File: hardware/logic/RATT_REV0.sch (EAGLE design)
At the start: 97 parts, among them IC1 TLP292-4, J3 F-1X06-SIP-100-40, J5 F-1X02-SIP-100-40, Q1 2.5A/30V, Q2 MBT3904DW1T1, Q3 2.5A/30V, Q5 2N7002, Q6 2.5A/30V, U3 MCP73831, U5 AP2112K-3.3V, U6 PCA9539PW

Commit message: All sorts of shit
I/Os are done, connectors, protections, options all added.  Screen updated, library updated, very close to layout ready.
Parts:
- added D10, D2, D5, D6, D7, D8, D9: BAT54S, DURRIDGE-DIODES:BAT54S
- added IC2, IC3, IC4, IC5: CPC1002N, MakeItLabs:CPC1002N
- added J1, J2, J4, J6: (no value), MakeItLabs:GROVE-CONNECTOR-TH-RA
- added J7, J8: PHOENIX1803484, MakeItLabs:PHOENIX1803484
- added JP1: (no value), pinhead:PINHD-2X8
- added LED1, LED2: (no value), SparkFun-LED:LED5MM
- added LED3: RED, SparkFun-LED:LED-RED0603
- added R41, R42: 680R, SparkFun-Resistors:RESISTOR0603-RES
- added R43, R44, R45, R46, R47, R48, R49, R50: 100R, SparkFun-Resistors:RESISTOR0603-RES
- added R51, R52, R53, R54: 680R, SparkFun-Passives:RESISTOR0603-RES
- D3: value RED -> BAT54S; device SparkFun-LED:LED-RED0603 -> DURRIDGE-DIODES:BAT54S
- LCD1: device MakeIt_Labs:1.8TFT_ADA -> MakeItLabs:1.8TFT_ADA
- LCD3: device MakeIt_Labs:1.8TFT_CHI2.0 -> MakeItLabs:1.8TFT_CHI2.0
- renumbered U$1 to U1, U3 to IC13, U6 to IC16
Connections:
- new net N$48: LED1.A, R41.1
- new net N$49: LED2.A, R42.1
- new net N$50: J2.1, R43.2
- new net N$51: J2.2, R44.2
- new net N$52: J1.1, R45.2
- new net N$53: J1.2, R46.2
- new net N$54: J4.1, R47.2
- new net N$55: J4.2, R48.2
- new net N$56: J6.1, R49.2
- new net N$57: J6.2, R50.2
- new net N$58: IC2.ANODE, R51.1
- new net N$59: IC2.DC+, J8.1.1
- new net N$60: IC2.DC-, J8.2.1
- new net N$61: IC3.ANODE, R52.1
- new net N$62: IC3.DC+, J8.3.1
- new net N$63: IC3.DC-, J8.4.1
- new net N$64: IC4.DC+, J8.5.1
- new net N$65: IC4.DC-, J8.6.1
- new net N$66: IC5.DC+, J8.7.1
- new net N$67: IC5.DC-, J8.8.1
- new net N$68: IC4.ANODE, R53.1
- new net N$69: IC5.ANODE, R54.1
- net +3V3: now also JP1.3, R41.2, R42.2
- net +5V: now also D10.C2, D2.C2, D3.C2, D5.C2, D6.C2, D7.C2, D8.C2, D9.C2, J1.3, J2.3, J4.3, J6.3, JP1.5
- net GND: now also D10.A1, D2.A1, D3.A1, D5.A1, D6.A1, D7.A1, D8.A1, D9.A1, IC2.CATHODE, IC3.CATHODE, IC4.CATHODE, IC5.CATHODE, J1.4, J2.4, J4.4, J6.4, JP1.1, JP1.7, LED3.C; no longer D3.C
- net I2C_SCL: now also JP1.9
- net I2C_SDA: now also JP1.11
- net IN0: now also D6.C1A2, JP1.2, R45.1
- net IN1: now also D5.C1A2, JP1.4, R46.1
- net IN2: now also D3.C1A2, JP1.6, R43.1
- net IN3: now also D2.C1A2, JP1.8, R44.1
- net LED0: now also LED1.C
- net LED1: now also LED2.C
- net N$11: now also LED3.A; no longer D3.A
- net N$40: now also J7.4.1
- net N$41: now also J7.3.1
- net N$42: now also J7.2.1
- net N$43: now also J7.1.1
- net N$44: now also J7.5.1
- net N$45: now also J7.6.1
- net N$46: now also J7.7.1
- net N$47: now also J7.8.1
- net OUT0: now also D8.C1A2, JP1.10, R47.1, R51.2
- net OUT1: now also D7.C1A2, JP1.12, R48.1, R52.2
- net OUT2: now also D10.C1A2, JP1.14, R49.1, R53.2
- net OUT3: now also D9.C1A2, JP1.16, R50.1, R54.2
- net RFID_RX: now also JP1.15
- net RFID_TX: now also JP1.13
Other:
- note added: "TODO: Revise power path circuit"
- note removed: "TODO: 2x LEDs I/O headers Revise power path circuit"
- moved on the sheet: IC1A, IC1B, IC1C, IC1D, R13, R14, R15, R16, R2, R22, R23, R3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

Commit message: saturday ratt
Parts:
- removed J5: F-1X02-SIP-100-40, con-headers-jp:F-1X02-SIP-100-40
- removed LCD1: 1.8TFT_ADA, MakeItLabs:1.8TFT_ADA
- J1, J2, J4, J6: value (none) -> 4P-2.0; device MakeItLabs:GROVE-CONNECTOR-TH-RA -> MakeItLabs:GROVE-CONNECTOR-TH-VERT
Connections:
- removed net N$50: J2.1, R43.2
- removed net N$51: J2.2, R44.2
- removed net N$52: J1.1, R45.2
- removed net N$53: J1.2, R46.2
- removed net N$54: J4.1, R47.2
- removed net N$55: J4.2, R48.2
- removed net N$56: J6.1, R49.2
- removed net N$57: J6.2, R50.2
- removed net N$67: IC5.DC-, J8.8.1
- removed net RFID_W0: J3.5
- removed net RFID_W1: J3.6
- new net IN0P: J1.1, JP1.2, R45.2
- new net IN1P: J1.2, JP1.4, R46.2
- new net IN2P: J2.1, JP1.6, R43.2
- new net IN3P: J2.2, JP1.8, R44.2
- new net OUT0P: J4.1, JP1.10, R47.2
- new net OUT1P: J4.2, JP1.12, R48.2
- new net OUT2P: J6.1, JP1.14, R49.2
- new net OUT3P: J6.2, JP1.16, R50.2
- net +3V3: now also J3.3; no longer J3.1
- net 5V_RFID_TX: now also J3.5; no longer J5.2
- net GND: now also J3.1; no longer J3.2
- net IN0: no longer JP1.2
- net IN1: no longer JP1.4
- net IN2: no longer JP1.6
- net IN3: no longer JP1.8
- net N$26: no longer LCD1.VCC
- net N$27: no longer LCD1.RESET
- net N$28: no longer LCD1.D/C
- net N$29: no longer LCD1.TFT_CS
- net N$3: no longer LCD1.GND
- net N$30: no longer LCD1.MOSI
- net N$31: no longer LCD1.SCK
- net N$32: now also IC2.DC-, J8.1.1; no longer LCD1.MISO, SJ10.1
- net N$33: no longer LCD1.LITE
- net N$59: now also J8.2.1; no longer J8.1.1
- net N$60: now also IC5.DC-, J8.7.1; no longer IC2.DC-, J8.2.1
- net N$62: now also IC5.DC+, J8.8.1; no longer IC3.DC+, J8.3.1
- net N$63: now also IC4.DC-, J8.5.1; no longer IC3.DC-, J8.4.1
- net N$64: now also J8.6.1; no longer J8.5.1
- net N$65: now also IC3.DC-, J8.3.1; no longer IC4.DC-, J8.6.1
- net N$66: now also IC3.DC+, J8.4.1; no longer IC5.DC+, J8.7.1
- net OUT0: no longer JP1.10
- net OUT1: no longer JP1.12
- net OUT2: no longer JP1.14
- net OUT3: no longer JP1.16
- net RFID_RX: now also J3.6; no longer J3.4
- net RFID_TX: no longer J3.3
- net V_USB: now also J3.2; no longer J5.1
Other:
- moved on the sheet: C21, C25, J1, J2, J4, J6, J8.1, J8.2, J8.3, J8.4, J8.5, J8.6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

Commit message: psuedo-routing
psuedo-routing to figure out final routing plan
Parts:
- removed SJ10: JUMPER-PAD-2-NC_BY_TRACE, SparkFun-Passives:JUMPER-PAD-2-NC_BY_TRACE
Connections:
- net 3V3@2 renamed 3V3
- removed net GND@3: U1.GND@1, U1.GND@2, U1.GND@3
- removed net GND@6: U1.GND@4, U1.GND@5, U1.GND@6, U1.GND@7, U1.GND@8
- net GND: now also U1.GND@1, U1.GND@2, U1.GND@3, U1.GND@4, U1.GND@5, U1.GND@6, U1.GND@7, U1.GND@8
- net LCD_MISO: no longer SJ10.2
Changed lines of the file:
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@@
 <setting verticaltext="up"/>
 </settings>
-<grid distance="0.1" unitdist="inch" unit="inch" style="lines" multiple="1" display="yes" altdistance="0.01" altunitdist="inch" altunit="inch"/>
+<grid distance="0.1" unitdist="inch" unit="inch" style="lines" multiple="1" display="no" altdistance="0.01" altunitdist="inch" altunit="inch"/>
 <layers>
 <layer number="1" name="Top" color="4" fill="1" visible="no" active="no"/>
@@
 <part name="SJ8" library="SparkFun-Passives" deviceset="JUMPER-PAD-2-NC_BY_TRACE" device="" value="JUMPER-PAD-2-NC_BY_TRACE"/>
 <part name="SJ9" library="SparkFun-Passives" deviceset="JUMPER-PAD-2-NC_BY_TRACE" device="" value="JUMPER-PAD-2-NC_BY_TRACE"/>
-<part name="SJ10" library="SparkFun-Passives" deviceset="JUMPER-PAD-2-NC_BY_TRACE" device="" value="JUMPER-PAD-2-NC_BY_TRACE"/>
 <part name="SJ11" library="SparkFun-Passives" deviceset="JUMPER-PAD-2-NC_BY_TRACE" device="" value="JUMPER-PAD-2-NC_BY_TRACE"/>
 <part name="SUPPLY55" library="supply2" deviceset="GND" device=""/>
@@
 <attribute name="NAME" x="35.56" y="144.78" size="1.778" layer="95" rot="R180"/>
 </instance>
-<instance part="SJ10" gate="G$1" x="33.02" y="144.78" smashed="yes" rot="R180">
-<attribute name="NAME" x="35.56" y="142.24" size="1.778" layer="95" rot="R180"/>
-</instance>
 <instance part="SJ11" gate="G$1" x="33.02" y="142.24" smashed="yes" rot="R180">
 <attribute name="NAME" x="35.56" y="139.7" size="1.778" layer="95" rot="R180"/>
@@
 </net>
 <net name="LCD_MISO" class="0">
-<segment>
-<wire x1="27.94" y1="144.78" x2="22.86" y2="144.78" width="0.1524" layer="91"/>
-<label x="22.86" y="144.78" size="1.27" layer="95" rot="R180" xref="yes"/>
-<pinref part="SJ10" gate="G$1" pin="2"/>
-</segment>
 <segment>
 <wire x1="27.94" y1="231.14" x2="22.86" y2="231.14" width="0.1524" layer="91"/>
@@
 <wire x1="271.78" y1="27.94" x2="271.78" y2="35.56" width="0.1524" layer="91"/>
 <junction x="271.78" y="35.56"/>
+</segment>
+<segment>
+<pinref part="U1" gate="G$1" pin="GND@3"/>
+<pinref part="SUPPLY10" gate="GND" pin="GND"/>
+<wire x1="27.94" y1="208.28" x2="25.4" y2="208.28" width="0.1524" layer="91"/>
+<wire x1="25.4" y1="208.28" x2="25.4" y2="205.74" width="0.1524" layer="91"/>
+<wire x1="25.4" y1="208.28" x2="25.4" y2="226.06" width="0.1524" layer="91"/>
+<junction x="25.4" y="208.28"/>
+<pinref part="U1" gate="G$1" pin="GND@2"/>
+<wire x1="25.4" y1="226.06" x2="27.94" y2="226.06" width="0.1524" layer="91"/>
+<wire x1="25.4" y1="226.06" x2="25.4" y2="246.38" width="0.1524" layer="91"/>
+<junction x="25.4" y="226.06"/>
+<pinref part="U1" gate="G$1" pin="GND@1"/>
+<wire x1="25.4" y1="246.38" x2="27.94" y2="246.38" width="0.1524" layer="91"/>
+</segment>
+<segment>
+<pinref part="SUPPLY9" gate="GND" pin="GND"/>
+<wire x1="78.74" y1="205.74" x2="78.74" y2="215.9" width="0.1524" layer="91"/>
+<pinref part="U1" gate="G$1" pin="GND@8"/>
+<wire x1="78.74" y1="215.9" x2="78.74" y2="220.98" width="0.1524" layer="91"/>
+<wire x1="78.74" y1="220.98" x2="78.74" y2="233.68" width="0.1524" layer="91"/>
+<wire x1="78.74" y1="233.68" x2="78.74" y2="241.3" width="0.1524" layer="91"/>
+<wire x1="78.74" y1="241.3" x2="78.74" y2="251.46" width="0.1524" layer="91"/>
+<wire x1="78.74" y1="251.46" x2="76.2" y2="251.46" width="0.1524" layer="91"/>
+<pinref part="U1" gate="G$1" pin="GND@7"/>
+<wire x1="76.2" y1="215.9" x2="78.74" y2="215.9" width="0.1524" layer="91"/>
+<junction x="78.74" y="215.9"/>
+<pinref part="U1" gate="G$1" pin="GND@5"/>
+<wire x1="76.2" y1="233.68" x2="78.74" y2="233.68" width="0.1524" layer="91"/>
+<junction x="78.74" y="233.68"/>
+<pinref part="U1" gate="G$1" pin="GND@4"/>
+<wire x1="76.2" y1="241.3" x2="78.74" y2="241.3" width="0.1524" layer="91"/>
+<junction x="78.74" y="241.3"/>
+<pinref part="U1" gate="G$1" pin="GND@6"/>
+<wire x1="76.2" y1="220.98" x2="78.74" y2="220.98" width="0.1524" layer="91"/>
+<junction x="78.74" y="220.98"/>
 </segment>
 </net>
@@
 </segment>
 </net>
-<net name="GND@3" class="0">
-<segment>
-<pinref part="U1" gate="G$1" pin="GND@3"/>
-<pinref part="SUPPLY10" gate="GND" pin="GND"/>
-<wire x1="27.94" y1="208.28" x2="25.4" y2="208.28" width="0.1524" layer="91"/>
-<wire x1="25.4" y1="208.28" x2="25.4" y2="205.74" width="0.1524" layer="91"/>
-<wire x1="25.4" y1="208.28" x2="25.4" y2="226.06" width="0.1524" layer="91"/>
-<junction x="25.4" y="208.28"/>
-<pinref part="U1" gate="G$1" pin="GND@2"/>
-<wire x1="25.4" y1="226.06" x2="27.94" y2="226.06" width="0.1524" layer="91"/>
-<wire x1="25.4" y1="226.06" x2="25.4" y2="246.38" width="0.1524" layer="91"/>
-<junction x="25.4" y="226.06"/>
-<pinref part="U1" gate="G$1" pin="GND@1"/>
-<wire x1="25.4" y1="246.38" x2="27.94" y2="246.38" width="0.1524" layer="91"/>
-</segment>
-</net>
 <net name="PWR_LOSS" class="0">
 <segment>
@@
 </segment>
 </net>
-<net name="GND@6" class="0">
-<segment>
-<pinref part="SUPPLY9" gate="GND" pin="GND"/>
-<wire x1="78.74" y1="205.74" x2="78.74" y2="215.9" width="0.1524" layer="91"/>
-<pinref part="U1" gate="G$1" pin="GND@8"/>
-<wire x1="78.74" y1="215.9" x2="78.74" y2="220.98" width="0.1524" layer="91"/>
-<wire x1="78.74" y1="220.98" x2="78.74" y2="233.68" width="0.1524" layer="91"/>
-<wire x1="78.74" y1="233.68" x2="78.74" y2="241.3" width="0.1524" layer="91"/>
-<wire x1="78.74" y1="241.3" x2="78.74" y2="251.46" width="0.1524" layer="91"/>
-<wire x1="78.74" y1="251.46" x2="76.2" y2="251.46" width="0.1524" layer="91"/>
-<pinref part="U1" gate="G$1" pin="GND@7"/>
-<wire x1="76.2" y1="215.9" x2="78.74" y2="215.9" width="0.1524" layer="91"/>
-<junction x="78.74" y="215.9"/>
-<pinref part="U1" gate="G$1" pin="GND@5"/>
-<wire x1="76.2" y1="233.68" x2="78.74" y2="233.68" width="0.1524" layer="91"/>
-<junction x="78.74" y="233.68"/>
-<pinref part="U1" gate="G$1" pin="GND@4"/>
-<wire x1="76.2" y1="241.3" x2="78.74" y2="241.3" width="0.1524" layer="91"/>
-<junction x="78.74" y="241.3"/>
-<pinref part="U1" gate="G$1" pin="GND@6"/>
-<wire x1="76.2" y1="220.98" x2="78.74" y2="220.98" width="0.1524" layer="91"/>
-<junction x="78.74" y="220.98"/>
-</segment>
-</net>
-<net name="3V3@2" class="0">
+<net name="3V3" class="0">
 <segment>
 <pinref part="U1" gate="G$1" pin="3V3@1"/>

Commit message: Lots o' routing
Screen, Pi, audio, preliminary IO routed
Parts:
- added X2: (no value), Adafruit_MAX98357:TERMBLOCK_1X2
- C17: device SparkFun-Capacitors:CAP0805 -> MakeItLabs:CAP0805
- C21, C25, C5, C6: device SparkFun-Capacitors:CAP0603-CAP -> MakeItLabs:CAP0603
- C9: device SparkFun-Passives:CAP0603-CAP -> MakeItLabs:CAP0603
- R13, R2, R25, R26, R27, R28, R29, R3, R30, R31, R32, R33, R34, R4, R41, R42, R43, R44, R45, R46, R47, R48, R49, R50, R6, R7: device SparkFun-Resistors:RESISTOR0603-RES -> MakeItLabs:RESISTOR0603
- R20, R37: device SparkFun-Resistors:2.0KOHM1/10W5%(0603) -> MakeItLabs:RESISTOR0603
- R23, R35, R38, R39, R40, R51, R52, R53, R54: device SparkFun-Passives:RESISTOR0603-RES -> MakeItLabs:RESISTOR0603
- R8: value 500K -> 680K; device SparkFun-Resistors:RESISTOR0603-RES -> MakeItLabs:RESISTOR0603
- SJ11, SJ3, SJ4, SJ5, SJ6, SJ7, SJ8, SJ9: device SparkFun-Passives:JUMPER-PAD-2-NC_BY_TRACE -> MakeItLabs:SOLDERJUMPER_CLOSED10MIL
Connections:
- removed net !LED0: U1.GPIO5
- removed net N$13: U1.!CE!/GPIO7
- net +3V3: no longer R8.2
- net +5V: now also X2.1
- net 5V_RFID_TX: now also J3.6; no longer J3.5
- net GND: now also X2.2
- net LCD_BACKLIGHT: now also U1.GPIO5; no longer U1.GEN4/GPIO23
- net LCD_RESET: now also U1.GEN4/GPIO23; no longer U1.GEN/6GPIO25
- net RFID_RX: now also J3.5; no longer J3.6
- net VIN: now also R8.2
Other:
- moved on the sheet: LCD3, Q5, R35

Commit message: Lot's O' routin'
Board resized to 3x5"
I/O 100% placed and routed
LEDs placed and routed
I/O chip routed
Todo: Power stuff
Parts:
- removed C1, C3: 0.1uF, SparkFun-Capacitors:CAP0603-CAP
- removed C2: 10uF, SparkFun-Capacitors:CAP0805
- removed R5: 10K, SparkFun-Resistors:RESISTOR0603-RES
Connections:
- removed net N$8: C2.1, R5.2
- removed net ~RESET: C3.1
- net !I/O_IRQ: now also U1.GPIO17/GEN0; no longer U1.GPIO4/GCKL
- net !I/O_RESET: now also U1.GPIO4/GCKL; no longer U1.GPIO17/GEN0
- net +3V3: now also JP1.8; no longer JP1.3
- net +5V: now also JP1.6; no longer JP1.5
- net GND: now also JP1.2, JP1.4; no longer C2.2, C3.2, JP1.1, JP1.7
- net I2C_SCL: now also JP1.15; no longer JP1.9
- net I2C_SDA: now also JP1.13; no longer JP1.11
- net IN0P: now also JP1.16; no longer JP1.2
- net IN1P: now also JP1.14; no longer JP1.4
- net IN2P: now also JP1.12; no longer JP1.6
- net IN3P: now also JP1.10; no longer JP1.8
- net OUT0P: now also JP1.1; no longer JP1.10
- net OUT1P: now also JP1.3; no longer JP1.12
- net OUT2P: now also JP1.5; no longer JP1.14
- net OUT3P: now also JP1.7; no longer JP1.16
- net RFID_RX: now also JP1.11; no longer JP1.15
- net RFID_TX: now also JP1.9; no longer JP1.13

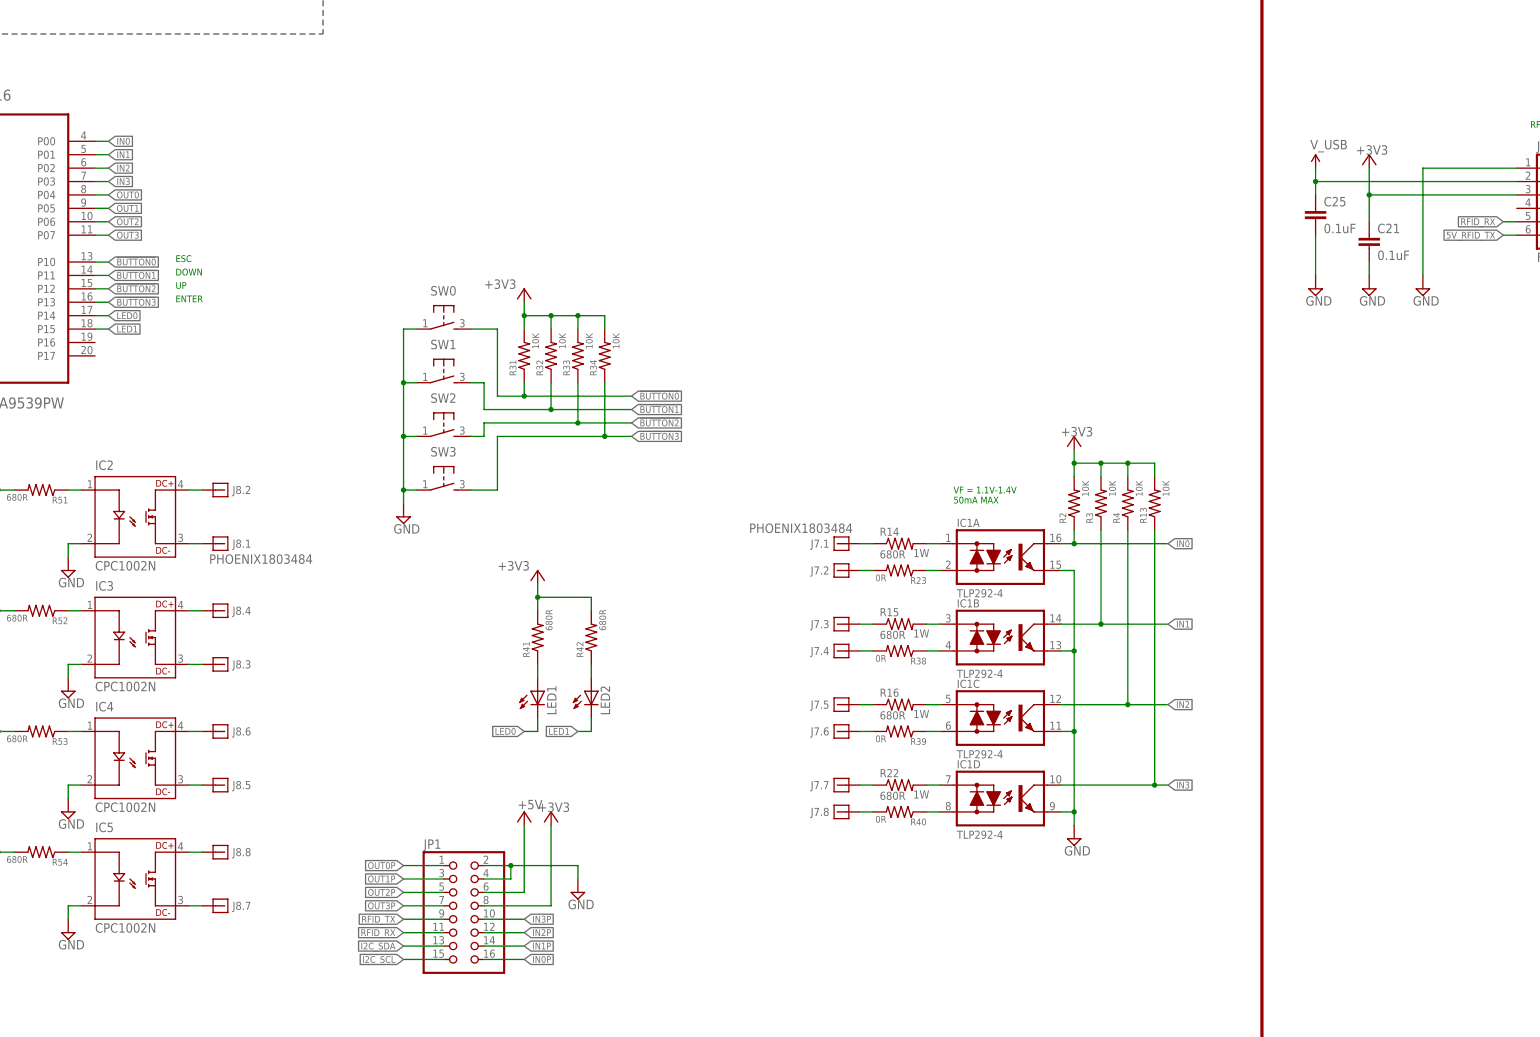
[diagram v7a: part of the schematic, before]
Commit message: A few tweaks on sch and brd
added PU to unused IO, added caps and beads to RFID power lines
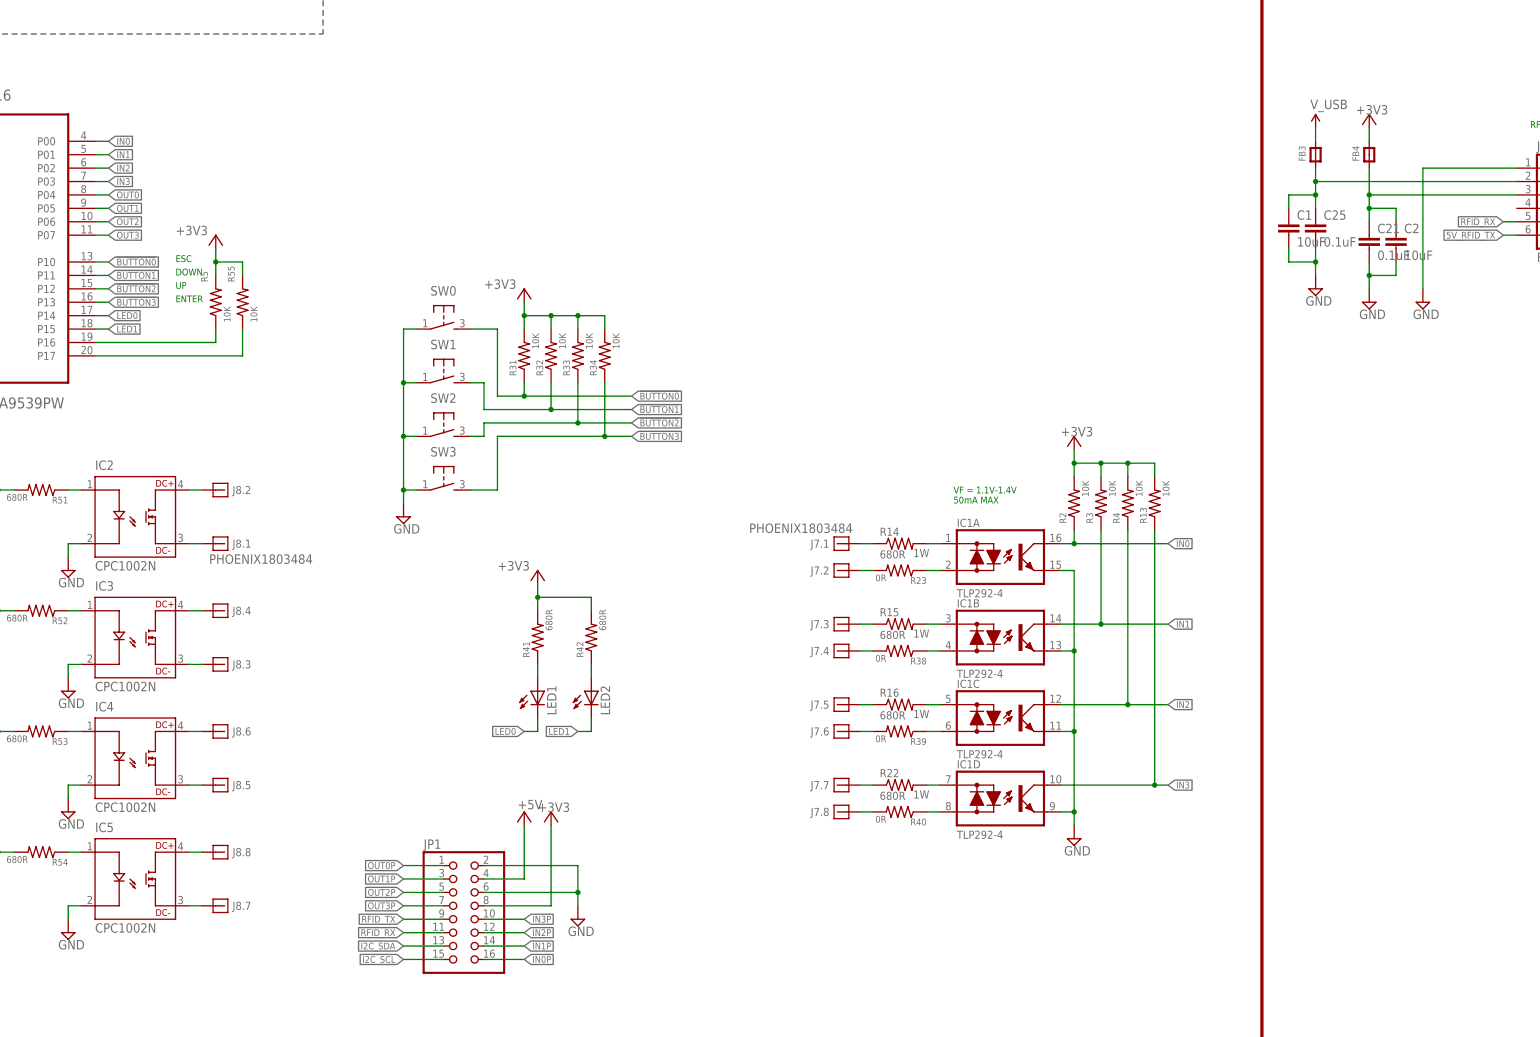
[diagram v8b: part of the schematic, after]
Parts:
- added C1, C2: 10uF, SparkFun-Capacitors:CAP0805
- added FB3, FB4: (no value), DURRIDGE-INDUCTORS:FERRITE
- added R5, R55: 10K, MakeItLabs:RESISTOR0603
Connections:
- new net N$13: IC16.P16, R5.1
- new net N$50: C2.1, C21.1, FB4.P$1, J3.3
- new net N$51: C1.1, C25.1, FB3.P$1, J3.2
- new net N$8: IC16.P17, R55.1
- net +3V3: now also FB4.P$2, R5.2, R55.2; no longer C21.1, J3.3
- net +5V: now also JP1.4; no longer JP1.6
- net GND: now also C1.2, C2.2, JP1.6; no longer JP1.4
- net V_USB: now also FB3.P$2; no longer C25.1, J3.2
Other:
- moved on the sheet: C25
